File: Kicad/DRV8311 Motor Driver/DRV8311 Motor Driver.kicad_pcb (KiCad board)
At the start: 4 copper layers, 15 x 15 mm, 21 parts, among them J1 1.27mm pin header, J11 Keystone 6102, J2 1.27mm pin header, J3 Keystone 6100, J4 Molex Picoblade, J5 Keystone 6102, J7 Keystone 6100, U1 DRV8311HRRWR

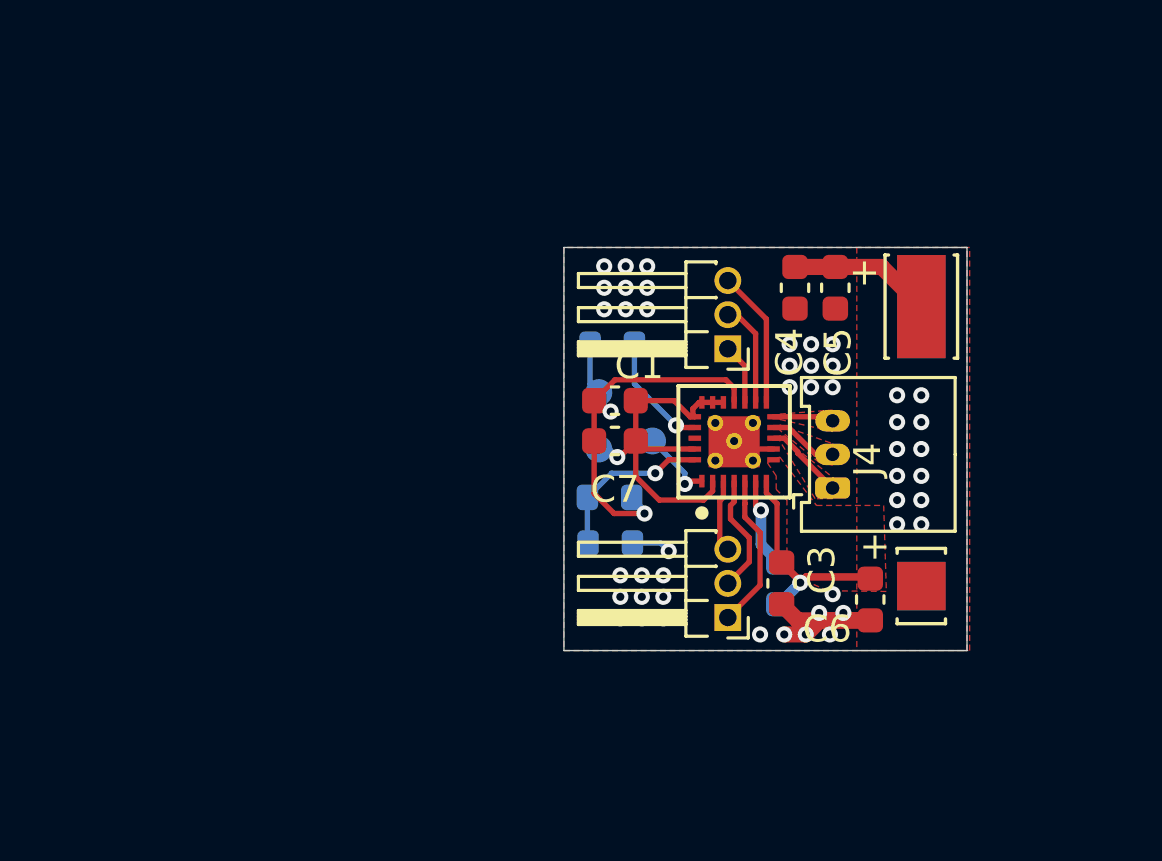
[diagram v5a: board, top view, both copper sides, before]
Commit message: Started switchout of motor power connectors
It looks like I may actually have gotten connectors a bit TOO big! I don't know if it will fit!
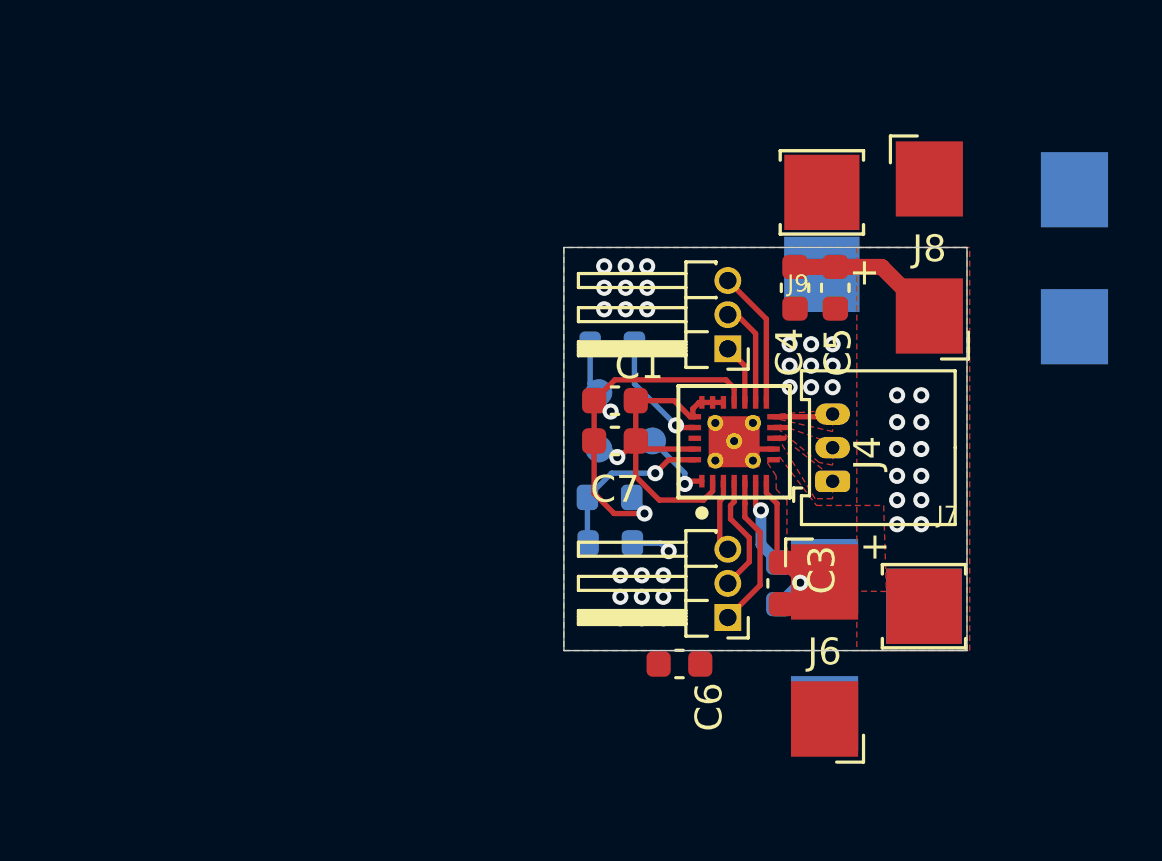
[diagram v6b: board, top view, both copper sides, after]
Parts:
- added J10: Keystone 3569, custom_Connector:Keystone_3569, B.Cu at (182.8, 94.6)
- added J6: Keystone 3569, custom_Connector:Keystone_3569, F.Cu at (173.5, 109.2)
- added J8: Keystone 3569, custom_Connector:Keystone_3569, F.Cu at (177.4, 94.2)
- added J9: Keystone 3579, custom_Connector:Keystone_3579, F.Cu at (173.4, 92.2)
- J11: value Keystone 6102 -> Keystone 3579; footprint 6102:KEYSTONE_6102 -> custom_Connector:Keystone_3579; moved to B.Cu
- J3, J7: value Keystone 6100 -> Keystone 3579; footprint 6100:KEYSTONE_6100 -> custom_Connector:Keystone_3579
- J5: value Keystone 6102 -> Keystone 3569; footprint 6102:KEYSTONE_6102 -> custom_Connector:Keystone_3569
- moved J5 13.1 mm to (173.5, 109.0), turned to 180 degrees
- moved C6 7.49 mm to (168.1, 109.7), turned to 0 degrees
- moved J11 3.89 mm to (173.4, 95.2), turned to 0 degrees
- moved J7 0.76 mm to (177.2, 107.5)
- moved J3 0.76 mm to (177.2, 107.5)
- moved J4 0.25 mm to (173.8, 102.9)
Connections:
- J11 pad 1: VDD -> GNDPWR
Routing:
- net GNDPWR: track 8.54 -> 1.58 mm, vias 34 -> 27
- net VDD: track 21.1 -> 18.3 mm
- net Net-(J4-Pin_1): track 3.00 -> 0.40 mm
- net Net-(J4-Pin_2): track 2.61 -> 0.57 mm

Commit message: Redesigned Motor Driver module for higher current
I doubled up the connectors on the edge, and I switched to a cheaper version of the same edge connector from Keystone. I'm planning on cutting the receptor in half because the male connector does not fully use the length, and I can save space and time. This is why the footprint is sticking off the edge
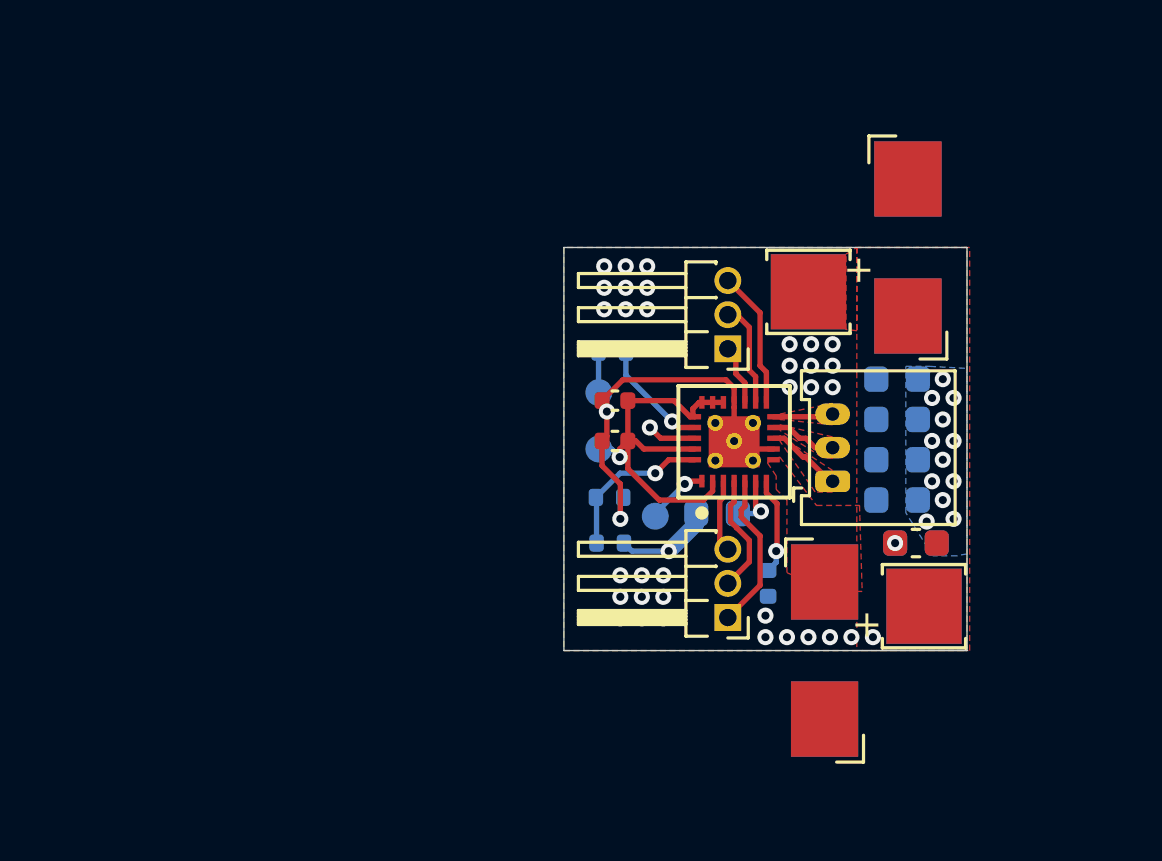
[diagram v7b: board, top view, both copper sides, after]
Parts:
- added C10: 10uF, 16v, Capacitor_SMD:C_0603_1608Metric, B.Cu at (176.9, 105.2)
- added C8: 10uF, 16v, Capacitor_SMD:C_0603_1608Metric, B.Cu at (176.2, 100.6)
- added C9: 10uF, 16v, Capacitor_SMD:C_0603_1608Metric, B.Cu at (176.2, 103.6)
- added NT1: NetTie_2, custom_Connector:NetTie-2_SMD_Pad0.2mm, F.Cu at (170.1, 100.3)
- C1: value 4.7uF -> 4.7uF, 10v; footprint Capacitor_SMD:C_0603_1608Metric -> Capacitor_SMD:C_0402_1005Metric
- C3: footprint Capacitor_SMD:C_0603_1608Metric -> Capacitor_SMD:C_0402_1005Metric; moved to B.Cu
- C4, C5: value 22uF, 16v -> 10uF, 16v; moved to B.Cu
- C7: value 0.1uF -> 0.1uF, 16v; footprint Capacitor_SMD:C_0603_1608Metric -> Capacitor_SMD:C_0402_1005Metric
- R1, R2, R3: footprint Resistor_SMD:R_0603_1608Metric -> Resistor_SMD:R_0402_1005Metric
- moved C6 9.88 mm to (176.9, 105.2), turned to 180 degrees
- moved C5 6.80 mm to (176.2, 102.1), turned to 180 degrees
- moved J10 6.21 mm to (176.6, 94.2)
- moved C4 5.10 mm to (176.2, 99.1), turned to 180 degrees
- moved J9 3.73 mm to (172.9, 95.8)
- moved C2 3.47 mm to (169.5, 104.1), turned to 180 degrees
- moved TP3 2.80 mm to (167.2, 104.2)
- moved J11 0.82 mm to (172.9, 95.8)
- moved J8 0.80 mm to (176.6, 94.2)
- moved C3 0.50 mm to (171.4, 106.7)
- moved R3 0.30 mm to (165.6, 98.1)
- moved J5 0.20 mm to (173.5, 109.2)
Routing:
- net VDD: track 18.3 -> 7.30 mm
- net Net-(J4-Pin_1): track 0.40 -> 2.86 mm
- net GND: track 16.2 -> 14.0 mm
- net Net-(J4-Pin_2): track 0.57 -> 2.51 mm
- net unconnected-(U1-SLEW-Pad22): track 0.00 -> 1.84 mm, vias 0 -> 1
- net Net-(U1-CP): track 3.39 -> 2.10 mm
- net +3.3V: track 14.6 -> 15.2 mm
- net GNDPWR: vias 27 -> 35
- added copper zone on B.Cu, net VDD
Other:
- board text added: "3v3"
- board text added: "<20A"
- board text added: "Fault"
- board text added: "GND"

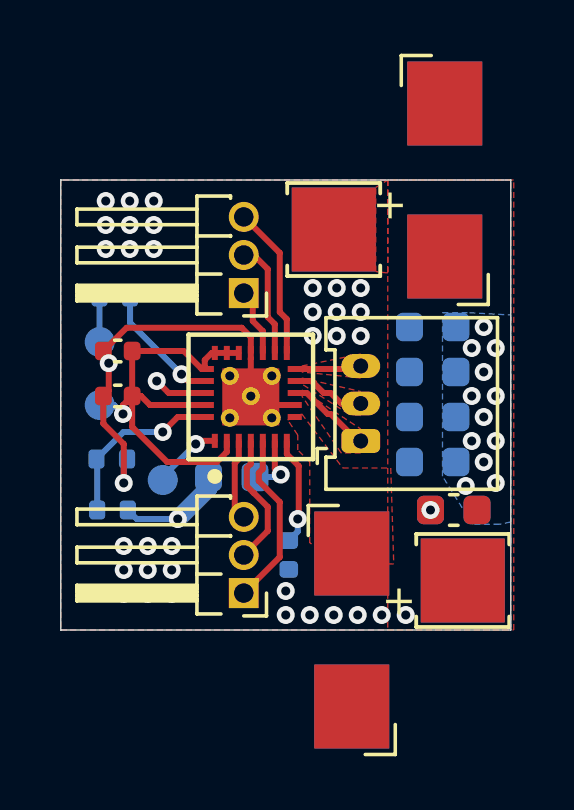
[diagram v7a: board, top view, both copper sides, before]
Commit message: Adjusted copper zones
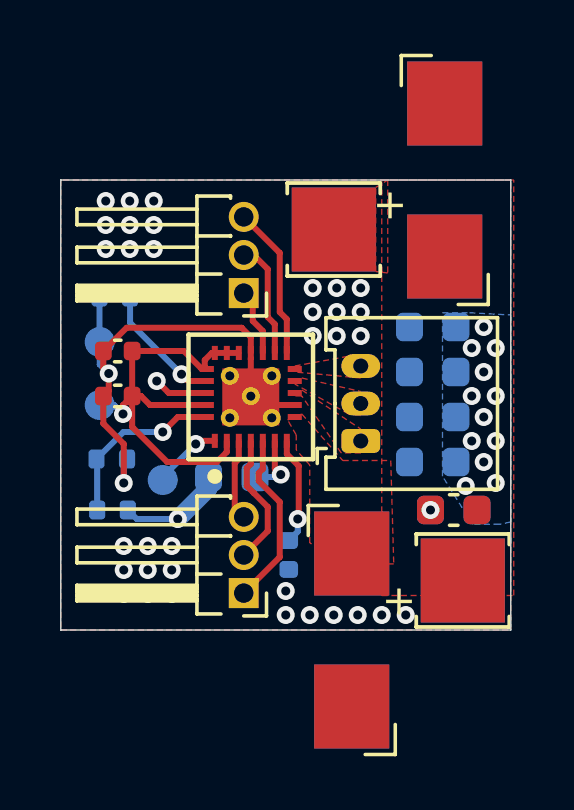
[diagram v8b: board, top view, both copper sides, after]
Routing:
- net Net-(J4-Pin_1): track 2.86 -> 0.10 mm
- net Net-(J4-Pin_2): track 2.51 -> 0.00 mm
- net Net-(J4-Pin_3): track 2.24 -> 0.14 mm
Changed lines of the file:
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@@
-	)
-	(segment
-		(start 165.22 99.9)
-		(end 165.22 100.126092)
-		(width 0.2)
-		(layer "F.Cu")
-		(net 2)
-	)
-	(segment
-		(start 165.4 100.306092)
-		(end 165.4 101.22)
-		(width 0.2)
-		(layer "F.Cu")
-		(net 2)
 	)
 	(segment
@@
 	)
 	(segment
+		(start 165.22 100.47)
+		(end 165.22 99.9)
+		(width 0.2)
+		(layer "F.Cu")
+		(net 2)
+	)
+	(segment
+		(start 165.4 100.65)
+		(end 165.4 101.22)
+		(width 0.2)
+		(layer "F.Cu")
+		(net 2)
+	)
+	(segment
 		(start 170.134999 99.43)
 		(end 169.829999 99.125)
@@
 	)
 	(segment
+		(start 165.995 99.125)
+		(end 165.22 99.9)
+		(width 0.2)
+		(layer "F.Cu")
+		(net 2)
+	)
+	(segment
+		(start 165.4 100.65)
+		(end 165.22 100.47)
+		(width 0.2)
+		(layer "F.Cu")
+		(net 2)
+	)
+	(segment
+		(start 165.4 100.65)
+		(end 165.331092 100.581092)
+		(width 0.2)
+		(layer "F.Cu")
+		(net 2)
+	)
+	(segment
+		(start 165.9 104.3)
+		(end 165.9 103)
+		(width 0.2)
+		(layer "F.Cu")
+		(net 2)
+	)
+	(segment
 		(start 165.4 101.22)
 		(end 165.22 101.4)
@@
 	)
 	(segment
-		(start 165.995 99.125)
-		(end 165.22 99.9)
-		(width 0.2)
-		(layer "F.Cu")
-		(net 2)
-	)
-	(segment
-		(start 165.22 100.126092)
-		(end 165.4 100.306092)
-		(width 0.2)
-		(layer "F.Cu")
-		(net 2)
-	)
-	(segment
-		(start 165.9 104.3)
-		(end 165.9 103)
-		(width 0.2)
-		(layer "F.Cu")
-		(net 2)
-	)
-	(segment
 		(start 169.829999 99.125)
 		(end 165.995 99.125)
@@
 	)
 	(segment
-		(start 165.4 100.306092)
-		(end 165.331092 100.306092)
-		(width 0.2)
-		(layer "F.Cu")
-		(net 2)
-	)
-	(segment
 		(start 170.134999 99.964998)
 		(end 170.134999 99.43)
@@
 	)
 	(via
-		(at 165.4 100.306092)
+		(at 165.4 100.65)
 		(size 0.6)
 		(drill 0.3)
@@
 	)
 	(segment
-		(start 165.4 100.306092)
-		(end 165.1 100.006092)
+		(start 165.4 100.65)
+		(end 165.1 100.35)
 		(width 0.2)
 		(layer "B.Cu")
@@
 	)
 	(segment
-		(start 165.1 100.006092)
-		(end 165.1 99.6)
-		(width 0.2)
-		(layer "B.Cu")
-		(net 2)
-	)
-	(segment
 		(start 165.9 103.61)
 		(end 166.01 103.5)
+		(width 0.2)
+		(layer "B.Cu")
+		(net 2)
+	)
+	(segment
+		(start 165.1 100.35)
+		(end 165.1 99.6)
 		(width 0.2)
 		(layer "B.Cu")
@@
 	)
 	(segment
-		(start 171.6 101.299999)
-		(end 171.999999 101.299999)
-		(width 0.2)
-		(layer "F.Cu")
-		(net 14)
-	)
-	(segment
-		(start 172.7 102)
-		(end 172.8 102)
-		(width 0.2)
-		(layer "F.Cu")
-		(net 14)
-	)
-	(segment
-		(start 172.8 102)
-		(end 173.7 102.9)
-		(width 0.2)
-		(layer "F.Cu")
-		(net 14)
-	)
-	(segment
 		(start 173.7 102.9)
 		(end 173.8 102.9)
@@
 	)
 	(segment
-		(start 171.999999 101.299999)
-		(end 172.7 102)
-		(width 0.2)
-		(layer "F.Cu")
-		(net 14)
-	)
-	(segment
-		(start 172.8 101.3)
-		(end 173.15 101.65)
-		(width 0.2)
-		(layer "F.Cu")
-		(net 15)
-	)
-	(segment
-		(start 171.6 100.9)
-		(end 172.165686 100.9)
-		(width 0.2)
-		(layer "F.Cu")
-		(net 15)
-	)
-	(segment
-		(start 172.165686 100.9)
-		(end 172.565686 101.3)
-		(width 0.2)
-		(layer "F.Cu")
-		(net 15)
-	)
-	(segment
-		(start 173.15 101.65)
-		(end 173.8 101.65)
-		(width 0.2)
-		(layer "F.Cu")
-		(net 15)
-	)
-	(segment
-		(start 172.565686 101.3)
-		(end 172.8 101.3)
-		(width 0.2)
-		(layer "F.Cu")
-		(net 15)
-	)
-	(segment
 		(start 168.669998 101.299999)
 		(end 167.399999 101.299999)
@@
 		(start 173.700002 100.499998)
 		(end 173.8 100.4)
-		(width 0.2)
-		(layer "F.Cu")
-		(net 17)
-	)
-	(segment
-		(start 171.6 100.499998)
-		(end 173.700002 100.499998)
 		(width 0.2)
 		(layer "F.Cu")
@@
 		(polygon
 			(pts
-				(xy 171.835 102) (xy 173.2 103.8) (xy 174.8 103.8) (xy 174.9 107) (xy 173.625 106.975) (xy 172.1 106.3)
-				(xy 172.1 103.6) (xy 171.7 103.2) (xy 171.7 102.7) (xy 171.365 102.2)
+				(xy 171.835 102) (xy 173.2 103.55) (xy 174.8 103.55) (xy 174.9 107) (xy 173.625 106.975) (xy 172.1 106.3)
+				(xy 172.1 103.7) (xy 171.65 103.2) (xy 171.65 102.7) (xy 171.365 102.2)
 			)
 		)
@@
 		(polygon
 			(pts
-				(xy 178.9 109.2) (xy 178.9 94.2) (xy 174.7 94.2) (xy 174.7 109.2)
+				(xy 178.9 108.05) (xy 178.9 94.2) (xy 174.5 94.2) (xy 174.5 108.05)
 			)
 		)
@@
 		(polygon
 			(pts
-				(xy 171.835 100.8) (xy 173.8 101.25) (xy 173.8 102.05) (xy 173.4 102) (xy 171.835 101)
+				(xy 171.835 100.8) (xy 173.8 101.25) (xy 173.8 102.05) (xy 173.4 102) (xy 171.6 101)
 			)
 		)
@@
 		(polygon
 			(pts
-				(xy 171.835 100.399998) (xy 173.8 100) (xy 173.8 100.8) (xy 171.835 100.599998)
+				(xy 171.6 100.399998) (xy 173.8 100) (xy 173.8 100.8) (xy 171.6 100.599998)
 			)
 		)
@@
 			(pts
 				(xy 171.835 101.199999) (xy 173.8 102.5) (xy 173.8 103.3) (xy 173.15 103.3) (xy 171.835 101.399999)
+				(xy 171.6 101.399999)
 			)
 		)
